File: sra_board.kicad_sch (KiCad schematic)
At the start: 162 parts, among them J1 Conn_01x14_Pin, J10 Conn_01x03_Pin, J11 Conn_01x03_Pin, J12 Conn_01x03_Pin, J13 MPU0650, J14 LSA, J15 OLED, J16 Conn_01x03_Pin, J17 Conn_01x03_Pin, J18 Conn_01x03_Pin, J3 Conn_01x08_Pin, J4 Conn_01x14_Pin, J5 USB_C_Receptacle_USB2.0_16P, J6 B2B-XH-A_LF__SN_, J7 B2B-XH-A_LF__SN_, J8 B2B-XH-A_LF__SN_, J9 Conn_01x03_Pin, Q1 SS8050, Q2 SS8050, Q3 AO3400A, Q4 AO3401A, Q5 AO3401A, Q6 AO3401A, Q7 AO3401A, SW1 SW_0, SW2 SW_EN, SW3 Switch, SW4 Switch, SW5 SW_Wuerth_450301014042, SW6 SW_Wuerth_450301014042, U1 MAX7219CWG_T, U2 CH340C, U3 TB6612FNG H-bridge Motor Driv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, U5 CN3303, U6 TPS562202, U7 ME6211C33M5, U8 ESP32-WROOM-32E

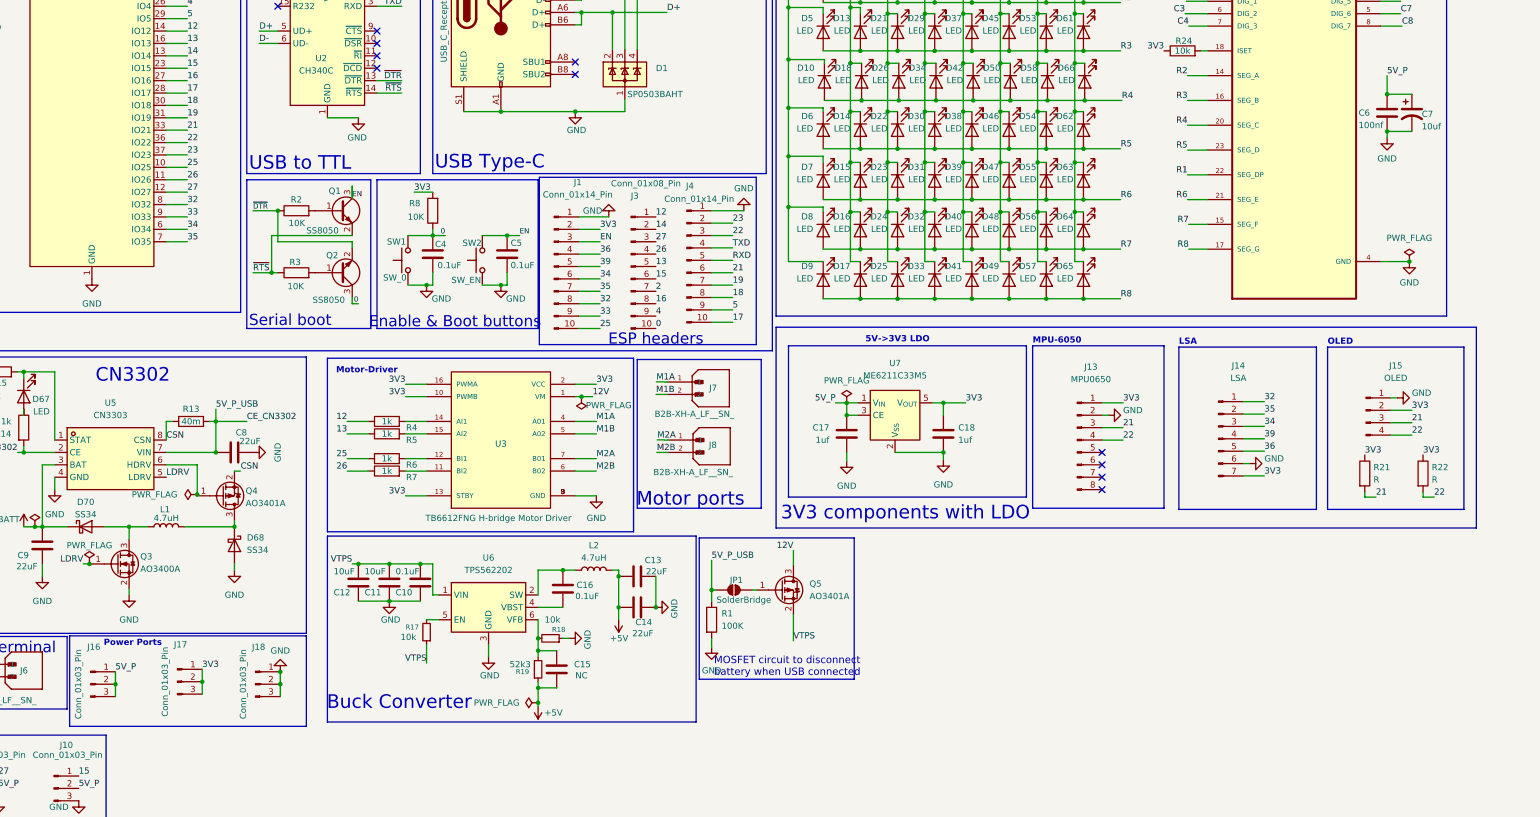
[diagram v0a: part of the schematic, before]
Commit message: Changing the buck converter IC and adding silkscreen and increasing thickness of traces
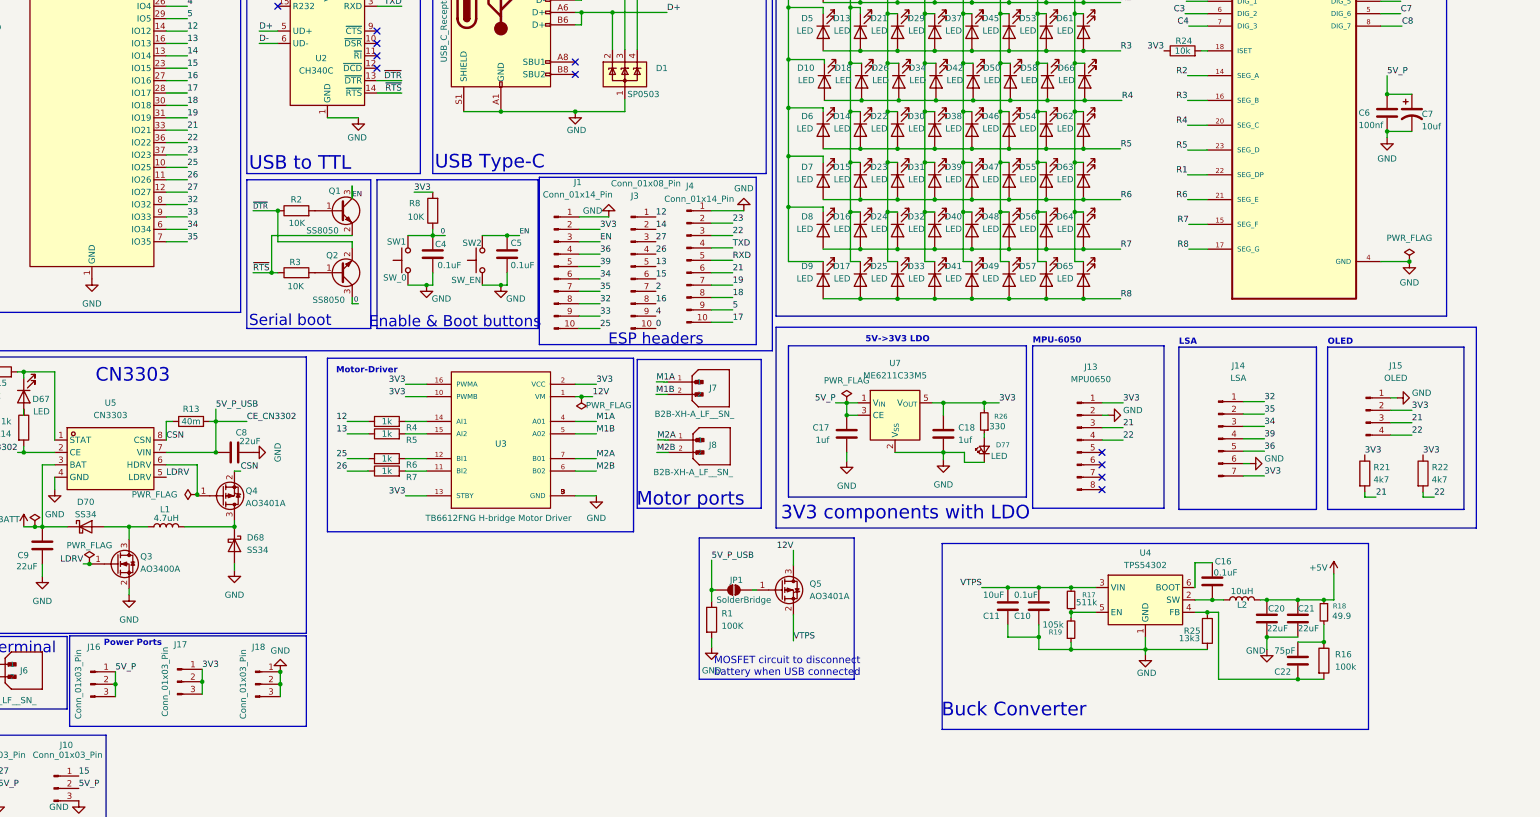
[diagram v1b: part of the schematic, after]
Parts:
- removed C12: 10uF, Capacitor_SMD:C_0805_2012Metric, symbol Device:C
- removed C13, C14: 22uF, Capacitor_SMD:C_0805_2012Metric, symbol Device:C
- removed C15: NC, Capacitor_SMD:C_0805_2012Metric, symbol Device:C
- removed U6: TPS562202, Package_TO_SOT_SMD:SOT-563, symbol Regulator_Switching:TPS562202
- added C20, C21: 22uF, Capacitor_SMD:C_1206_3216Metric, symbol Device:C
- added C22: 75pF, Capacitor_SMD:C_0805_2012Metric, symbol Device:C
- added D77: LED, LED_SMD:LED_0805_2012Metric, symbol Device:LED_Small
- added R16: 100k, Resistor_SMD:R_0805_2012Metric, symbol Device:R
- added R25: 13k3, Resistor_SMD:R_0805_2012Metric, symbol Device:R
- added R26: 330, Resistor_SMD:R_0805_2012Metric, symbol Device:R_Small
- added U4: TPS54302, Package_TO_SOT_SMD:SOT-23-6, symbol Regulator_Switching:TPS54302
- C10, C11: footprint Capacitor_SMD:C_0805_2012Metric -> Capacitor_SMD:C_1206_3216Metric
- D1: value SP0503BAHT -> SP0503
- D67, D69, D74, D76: footprint LED_SMD:LED_0603_1608Metric_Pad1.05x0.95mm_HandSolder -> LED_SMD:LED_0805_2012Metric
- L2: value 4.7uH -> 10uH; footprint Inductor_SMD:L_Sunlord_MWSA0603S -> Inductor_SMD:L_Sunlord_MWSA1004S
- R17: value 10k -> 511k
- R18: value 10k -> 49.9
- R19: value 52k3 -> 105k
- R21, R22: value R -> 4k7
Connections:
- net +5V: now also R18.1, C20.1, C21.1; no longer R19.1
- net 3V3: now also R26.2
- net GND: now also R19.1, C20.2, C21.2, D77.1 (K), R25.2, U4.1 (GND); no longer R18.1
- net VTPS: now also R17.2, U4.3 (VIN); no longer R17.1
- net at R18.2: now also C22.1, R16.1; no longer R19.2
- net at C16.1: now also U4.6 (BOOT); no longer L2.1
- net at C16.2: now also L2.1, U4.2 (SW)
- new net: D77.2 (A), R26.1
- new net: R17.1, R19.2, U4.5 (EN)
- new net: C22.2, R16.2, R25.1, U4.4 (FB)
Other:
- note added: "CN3303"
- note removed: "CN3302"
- moved on the sheet: C10, C11, C16, L2, R17, R18, R19

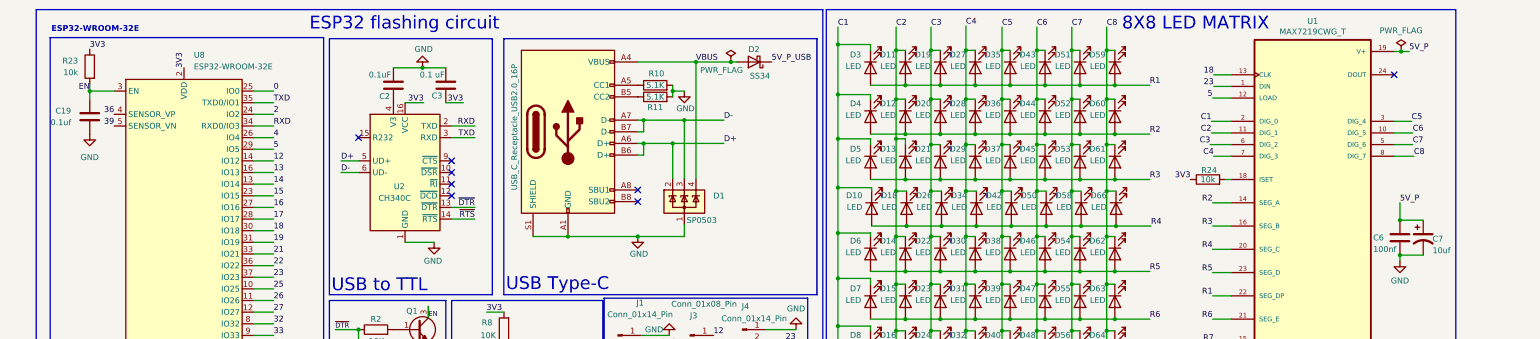
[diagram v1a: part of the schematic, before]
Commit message: Changed silkscreen and routing a bit
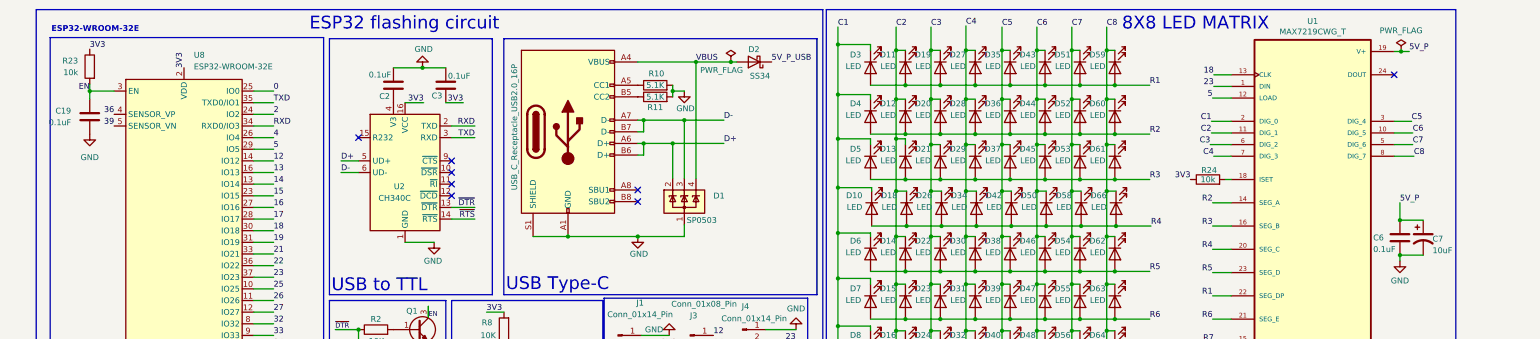
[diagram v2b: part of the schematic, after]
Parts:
- C19: value 0.1uf -> 0.1uF
- C3: value 0.1 uF -> 0.1uF
- C6: value 100nf -> 0.1uF
- C7: value 10uf -> 10uF
- U5: MANUFACTURER (none) -> CONSONANCE(上海如韵); Manufacturer CONSONANCE(上海如韵) -> (none)
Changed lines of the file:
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@@
 			)
 		)
-		(property "Value" "0.1 uF"
-			(at 102.87 27.686 0)
+		(property "Value" "0.1uF"
+			(at 108.458 27.94 0)
 			(show_name no)
 			(do_not_autoplace no)
@@
 			)
 		)
-		(property "Manufacturer" "CONSONANCE(上海如韵)"
+		(property "MANUFACTURER" "CONSONANCE(上海如韵)"
 			(at 49.784 150.622 0)
 			(hide yes)
@@
 			)
 		)
-		(property "Value" "0.1uf"
+		(property "Value" "0.1uF"
 			(at 21.336 38.0999 0)
 			(show_name no)
@@
 			)
 		)
-		(property "Value" "10uf"
+		(property "Value" "10uF"
 			(at 318.516 66.04 0)
 			(show_name no)
@@
 			)
 		)
-		(property "Value" "100nf"
+		(property "Value" "0.1uF"
 			(at 305.562 65.786 0)
 			(show_name no)

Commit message: Partial placing of components in PCB
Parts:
- removed C17, C18: 1uf, Capacitor_SMD:C_0805_2012Metric, symbol Device:C
- removed J6: B2B-XH-A_LF__SN_, Connector_JST:JST_EH_B2B-EH-A_1x02_P2.50mm_Vertical, symbol Power JST:B2B-XH-A_LF__SN_
- removed JP2, JP3, JP4, JP5: SolderBridge, Connector_PinHeader_2.54mm:PinHeader_1x02_P2.54mm_Vertical, symbol Jumper:SolderJumper_2_Open
- removed Q6, Q7: AO3401A, Package_TO_SOT_SMD:SOT-23, symbol Transistor_FET:AO3401A
- removed R12, R9: 100K, Resistor_SMD:R_0805_2012Metric, symbol Device:R
- removed R26: 330, Resistor_SMD:R_0805_2012Metric, symbol Device:R_Small
- removed SW3, SW4: Switch, Button_Switch_THT:SW_Push_2P2T_Toggle_CK_PVA2OAH5xxxxxxV2, symbol Switch:SW_Push_DPDT
- removed U7: ME6211C33M5, Package_TO_SOT_SMD:SOT-23-5, symbol Regulator_Linear:ME6211C33M5
- added C10, C12: 0.1uF, Capacitor_SMD:C_0805_2012Metric, symbol Device:C
- added C11: 10uF, Capacitor_SMD:C_0805_2012Metric, symbol Device:C
- added C13: 22uF, Capacitor_SMD:C_0805_2012Metric, symbol Device:C
- added C8, C9: 0.1uF, Capacitor_SMD:C_1206_3216Metric, symbol Device:C
- added H1, H2, H3, H4: MountingHole, MountingHole:MountingHole_3.2mm_M3_DIN965_Pad, symbol Mechanical:MountingHole
- added J1: Barrel_Jack, Connector_BarrelJack:BarrelJack_Wuerth_6941xx301002, symbol Connector:Barrel_Jack
- added R15: 330, Resistor_SMD:R_0805_2012Metric, symbol Device:R
- added U5: AMS1117-3.3, Package_TO_SOT_SMD:SOT-223-3_TabPin2, symbol Regulator_Linear:AMS1117-3.3
- J16: renamed from J14; footprint Connector_PinSocket_2.54mm:PinSocket_1x07_P2.54mm_Vertical -> Connector_FFC-FPC:JUSHUO_AFA07-S08FCA-00_1x8-1MP_P1.0mm_Horizontal; symbol Connector:Conn_01x07_Pin -> Connector:Conn_01x08_Pin
- L2: footprint Inductor_SMD:L_Sunlord_MWSA1004S -> Inductor_SMD:L_Sunlord_MWSA0618S
- R25: renamed from R50; value 680 -> 330
- renumbered C19 to C1, C11 to C14, C10 to C15, C6 to C16, C7 to C17, C16 to C18, C20 to C19, C9 to C2, C21 to C20, C22 to C21, C8 to C3, C2 to C4, C3 to C5, C4 to C6, C5 to C7, D69 to D1, D6 to D10, D7 to D11, D8 to D12, D9 to D13, D10 to D14, D11 to D15, D12 to D16, D13 to D17, D14 to D18, D15 to D19, D67 to D2, D16 to D20, D17 to D21, D18 to D22, D19 to D23, D20 to D24, D21 to D25, D22 to D26, D23 to D27, D24 to D28, D25 to D29, D70 to D3, D26 to D30, D27 to D31, D28 to D32, D29 to D33, D30 to D34, D31 to D35, D32 to D36, D33 to D37, D34 to D38, D35 to D39, D68 to D4, D36 to D40, D37 to D41, D38 to D42, D39 to D43, D40 to D44, D41 to D45, D42 to D46, D77 to D47, D43 to D48, D44 to D49, D1 to D5, D45 to D50, D46 to D51, D47 to D52, D48 to D53, D49 to D54, D50 to D55, D51 to D56, D52 to D57, D53 to D58, D54 to D59, D2 to D6, D55 to D60, D56 to D61, D57 to D62, D58 to D63, D59 to D64, D60 to D65, D61 to D66, D62 to D67, D63 to D68, D64 to D69, D3 to D7, D65 to D70, D66 to D71, D75 to D72, D76 to D74, D74 to D75, D4 to D8, D5 to D9, F2 to F1, F1 to F2, J8 to J10, J9 to J11, J10 to J12, J11 to J13, J13 to J14, J12 to J15, J15 to J17, J16 to J2, J5 to J3, J1 to J4, J17 to J5, J3 to J6, J18 to J7, J4 to J8, J7 to J9, Q3 to Q1, Q4 to Q2, Q1 to Q3, Q2 to Q4, R23 to R1, R7 to R10, R8 to R11, R10 to R12, R11 to R13, R1 to R14, R24 to R16, R19 to R18, R21 to R19, R15 to R2, R22 to R20, R25 to R21, R18 to R22, R16 to R23, R20 to R24, R14 to R3, R13 to R4, R2 to R5, R3 to R6, R4 to R7, R5 to R8, R6 to R9, SW6 to SW3, SW5 to SW4, U8 to U1, U5 to U2, U2 to U3, U3 to U4, U1 to U6, U4 to U7
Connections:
- net 12V_Switch is gone; now on an unnamed net: F2.2
- net 5V_Switch is gone; now on an unnamed net: F1.2
- net +BATT: now also J1.1
- net 12V: now also SW4.3 (A)
- net 32: now also J16.7 (Pin_7); no longer J16.1 (Pin_1)
- net 34: now also J16.5 (Pin_5); no longer J16.3 (Pin_3)
- net 35: now also J16.6 (Pin_6); no longer J16.2 (Pin_2)
- net 36: now also J16.3 (Pin_3); no longer J16.5 (Pin_5)
- net 3V3: now also J16.1 (Pin_1), C12.1, C13.1, R15.1, U5.2 (VO); no longer J16.7 (Pin_7)
- net 5V_P: now also SW3.3 (A), C10.1, C11.1, U5.3 (VI)
- net D+: now also D5.3 (K); no longer D5.2 (K)
- net D-: now also D5.2 (K); no longer D5.3 (K)
- net GND: now also J16.2 (Pin_2), C10.2, C11.2, C12.2, C13.2, J1.2, U5.1 (GND); no longer J16.6 (Pin_6), SW3.3 (A), SW4.3 (A)
- net M1A: now also C9.1
- net M1B: now also C9.2
- net M2A: now also C8.1
- net M2B: now also C8.2
- net at D47.2 (A): now also R15.2
- no-connect marks 18 -> 15
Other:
- note added: "Mounting Holes"
- moved on the sheet: C14, C15, C18, C19, C20, C21, D47, D72, D73, D74, D75, F1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

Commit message: Partial routing complete
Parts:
- removed JP1: SolderBridge, Connector_PinHeader_2.54mm:PinHeader_1x02_P2.54mm_Vertical, symbol Jumper:SolderJumper_2_Open
- removed Q5: AO3401A, Package_TO_SOT_SMD:SOT-23, symbol Transistor_FET:AO3401A
- removed R14: 100K, Resistor_SMD:R_0805_2012Metric, symbol Device:R
- H1, H2, H3, H4: footprint MountingHole:MountingHole_3.2mm_M3_DIN965_Pad -> MountingHole:MountingHole_3.2mm_M3_DIN965
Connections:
- net VTPS is gone; now on net 12V: C14.1, C15.1, R17.2, U7.3 (VIN)
- net 32: now also J16.8 (Pin_8); no longer J16.7 (Pin_7)
- net 34: now also J16.6 (Pin_6); no longer J16.5 (Pin_5)
- net 35: now also J16.7 (Pin_7); no longer J16.6 (Pin_6)
- net 36: now also J16.4 (Pin_4); no longer J16.3 (Pin_3)
- net 39: now also J16.5 (Pin_5); no longer J16.4 (Pin_4)
- net 3V3: now also J16.2 (Pin_2); no longer J16.1 (Pin_1)
- net D+: now also D5.2 (K); no longer D5.3 (K)
- net D-: now also D5.3 (K); no longer D5.2 (K)
- net GND: now also J16.3 (Pin_3); no longer J16.2 (Pin_2)
- net at SW4.1 (B): no longer F2.2
- net at SW4.2 (C): now also F2.2
- net at SW3.1 (B): no longer F1.2
- net at SW3.2 (C): now also F1.2
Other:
- note removed: "MOSFET circuit to disconnect battery when USB connected"
- moved on the sheet: D72, D73, F1, F2

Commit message: Adding new layout of pcb
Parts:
- removed F1: 1A, Fuse:Fuse_2920_7451Metric, symbol Device:Fuse
- removed R22: 49.9, Resistor_SMD:R_0805_2012Metric, symbol Device:R_Small
- added J18: B2B-XH-A_LF__SN_, Connector_JST:JST_EH_B2B-EH-A_1x02_P2.50mm_Vertical, symbol Power JST:B2B-XH-A_LF__SN_
- added Q7: ZXMP4A16GTA, Package_TO_SOT_SMD:SOT-223, symbol Transistor_FET:AO3401A
- added R14: 100K, Resistor_SMD:R_0805_2012Metric, symbol Device:R
- C21: value 75pF -> NC; now left out of the parts list
- D3, D4: value SS34 -> SS54
- D6: value SS34 -> SS54; footprint Diode_SMD:D_SMB -> Diode_SMD:D_SMA
- D72: value SS14 -> SS34; footprint Diode_SMD:D_SMA -> Diode_SMD:D_SMB
- L1: value 4.7uH -> 6.8uH
- L2: footprint Inductor_SMD:L_Sunlord_MWSA0618S -> Inductor_SMD:L_Sunlord_MWSA0603S
- Q1: value AO3400A -> DMN3016lss; footprint Package_TO_SOT_SMD:SOT-23 -> Package_SO:SOIC-8-1EP_3.9x4.9mm_P1.27mm_EP2.41x3.3mm_ThermalVias
- Q2: value AO3401A -> SI4435FDY; footprint Package_TO_SOT_SMD:SOT-23 -> Package_SO:SOIC-8-1EP_3.9x4.9mm_P1.27mm_EP2.41x3.3mm_ThermalVias
- R17: value 511k -> 10K
- R18: value 105k -> 4k7
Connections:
- net +5V is gone; now on an unnamed net: C19.1, C20.1, D72.2 (A), L2.2
- net +BATT: now also J18.2
- net 12V: now also Q7.3 (D); no longer SW4.3 (A)
- net 5V_P: now also D6.1 (K), D72.1 (K); no longer SW3.3 (A)
- net 5V_P_USB: no longer D6.1 (K), D72.1 (K)
- net EN: now also R17.1, R18.2, SW3.1 (B), U7.5 (EN)
- net GND: now also SW3.2 (C), SW4.2 (C), J18.1
- net at SW4.1 (B): now also Q7.1 (G), R14.1
- net at F2.2: now also D73.1 (K); no longer SW4.2 (C)
- net at F2.1: now also Q7.2 (S), R14.2; no longer D73.1 (K)
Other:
- note added: "Battery Switch"
- note added: "Buck converter EN switch"
- note removed: "Switches"
- moved on the sheet: D72, D73, D74, D75, F2, R24, R25, SW4

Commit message: Adding new fully routed PCB without CN3303 and controlling the EN pin of TPS with switch rather than actual power line
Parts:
- removed C2, C3: 22uF, Capacitor_SMD:C_1206_3216Metric, symbol Device:C
- removed D1, D2: LED, LED_SMD:LED_0805_2012Metric, symbol Device:LED
- removed D3, D4: SS54, Diode_SMD:D_SMA, symbol Diode:SS34
- removed L1: 6.8uH, Inductor_SMD:L_Sunlord_MWSA0603S, symbol Device:L
- removed Q1: DMN3016lss, Package_SO:SOIC-8-1EP_3.9x4.9mm_P1.27mm_EP2.41x3.3mm_ThermalVias, symbol Transistor_FET:AO3400A
- removed Q2: SI4435FDY, Package_SO:SOIC-8-1EP_3.9x4.9mm_P1.27mm_EP2.41x3.3mm_ThermalVias, symbol Transistor_FET:AO3401A
- removed R2, R3: 1k, Resistor_SMD:R_0805_2012Metric, symbol Device:R
- removed R4: 40m, Resistor_SMD:R_1206_3216Metric, symbol Device:R
- removed U2: CN3303, easyeda2kicad:SOP-8_L4.9-W3.9-P1.27-LS6.0-BL, symbol easyeda2kicad:CN3302
- D6: value SS54 -> SS14
- J3: footprint Connector_USB:USB_C_Receptacle_GCT_USB4105-xx-A_16P_TopMnt_Horizontal -> footprints:AMPHENOL_GSB1C4621DS1HR
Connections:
- net +BATT: now also J18.1; no longer J18.2
- net EN: no longer R17.1, R18.2, SW3.1 (B), U7.5 (EN)
- net GND: now also J18.2; no longer J18.1
- new net EN_TPS: R17.1, R18.2, SW3.1 (B), U7.5 (EN)
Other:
- note removed: "CN3303"
